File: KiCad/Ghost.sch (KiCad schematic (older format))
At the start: 33 parts, among them P1 MOTOR, P2 SERVO, P3 START, P4 PWM, P5 RGB, Q1 MMBT3904, SW1 BTN1, U1 INA219, U16 Transmissive_Photo_Interrupter, U17 ESP8266_ESP-12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

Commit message: Working on PCB layout for Rev 2
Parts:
- removed P4: PWM, Pin_Headers:Pin_Header_Straight_1x03, symbol CONN_01X03
- removed R27: 3k3, Resistors_SMD:R_0603, symbol R
- added P4: CONN_01X06, Pin_Headers:Pin_Header_Straight_1x06, symbol CONN_01X06
- added R9: 0, Resistors_SMD:R_0603, symbol R
- added SW2: PROG, Buttons_Switches_SMD:SW_SPST_SKQG, symbol SW_PUSH
- D1, D2, D3: footprint LEDs:LED_0805 -> LEDs:LED_0603
- Q1: symbol Q_NPN_BCE -> Q_NPN_BEC
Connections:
- net labels added: FTDI_CTS, FTDI_DTR, FTDI_RX, FTDI_TX, ~WIFI_RESET
- net labels removed: PWM
- wire segments 130 -> 138
- no-connect marks 32 -> 34
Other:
- note added: "Programming header for ESP8266\nUse FTDI Basic.\n0 ohm resistor acts as optional jumper for power."
- note added: "Toggle LEDs with one GPIO\nNPN is a MMBT3904, SOT-23."
- note added: "WiFi. Can be enabled/disabled from Teensy.\nUse pushbutton for firmware programming.\nNB, pull ~Reset~=HIGH and Enable=HIGH using Teensy."
- note removed: "General purpose PWM connector"
- note removed: "Toggle LEDs with one GPIO\nNPN is a MMB3904, SOT-23."
- note removed: "Wireless Network. Can be enabled/disabled."
- moved on the sheet: C2, C3, C9, P3, P5, R25, R26, R28, R29, U16, U3

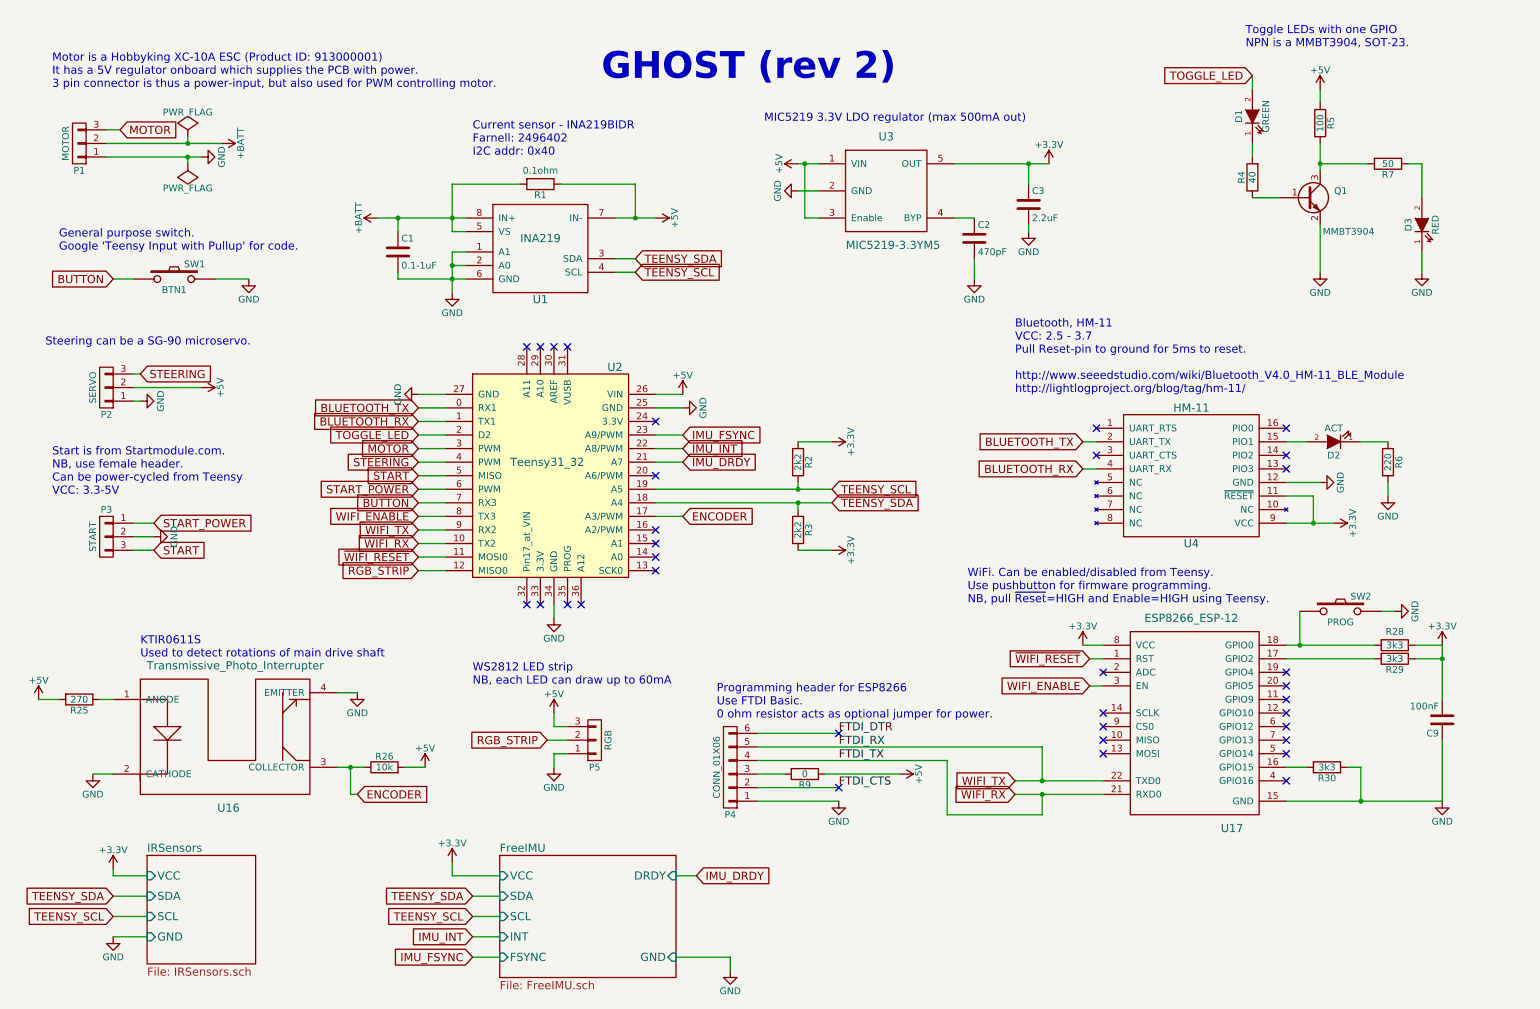
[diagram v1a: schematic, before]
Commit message: Replacing Teensy with ESP8266
Changes made on KiCad on Ubuntu
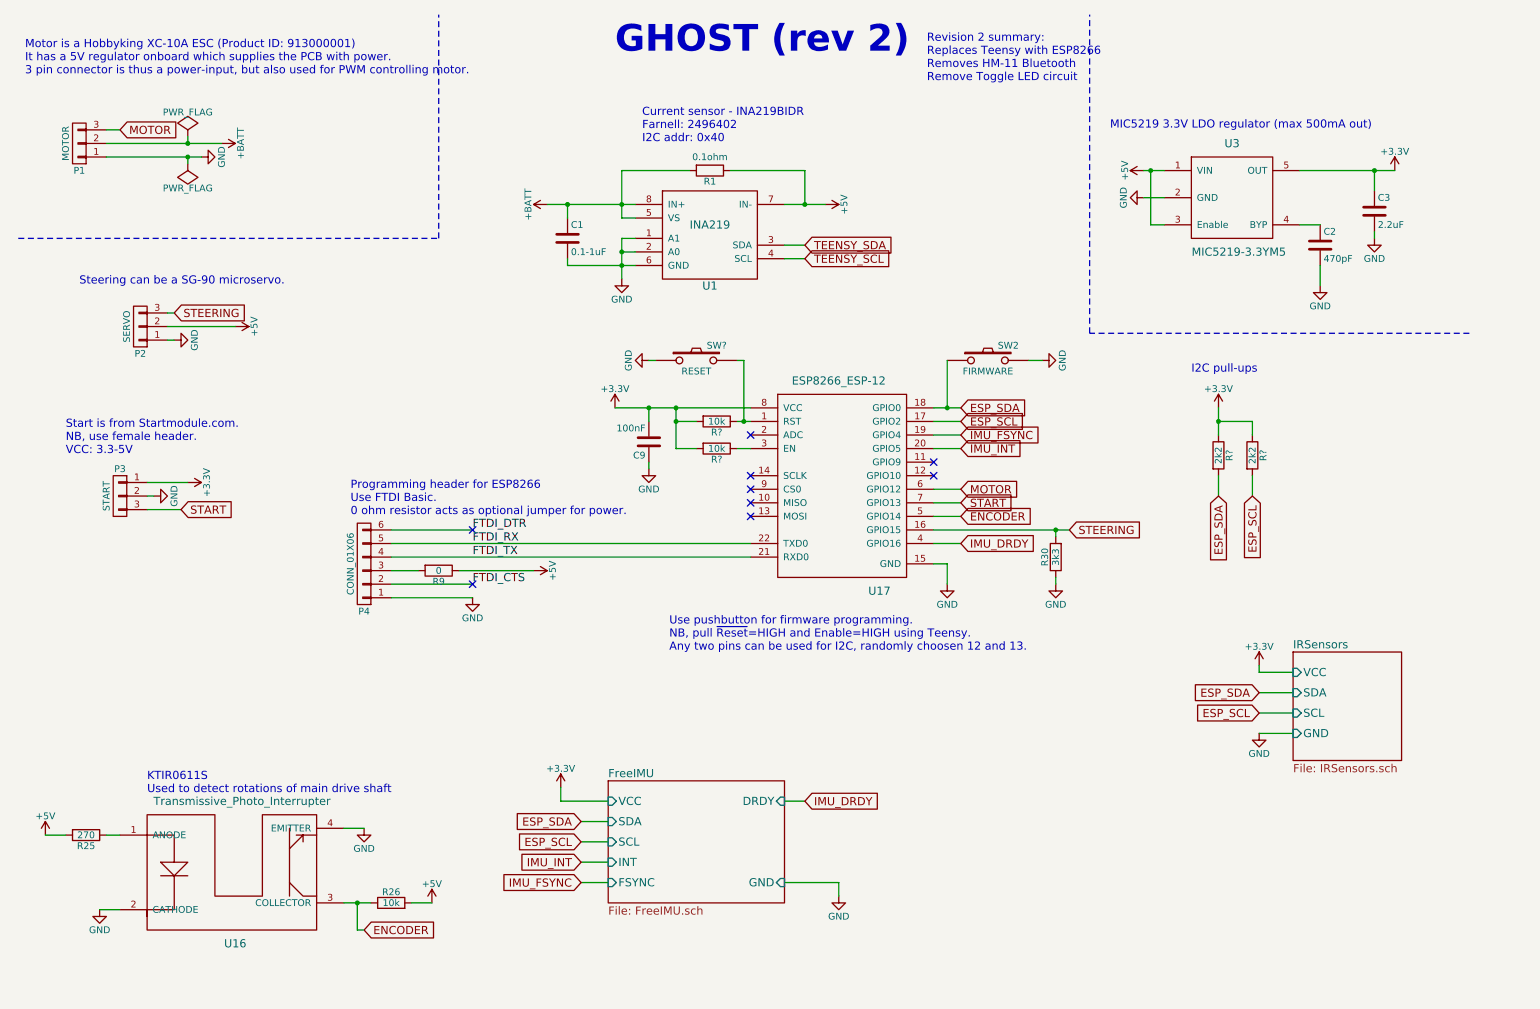
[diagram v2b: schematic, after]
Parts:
- removed D1: GREEN, LEDs:LED_0603, symbol LED
- removed D2: ACT, LEDs:LED_0603, symbol LED
- removed D3: RED, LEDs:LED_0603, symbol LED
- removed P5: RGB, Pin_Headers:Pin_Header_Straight_1x03, symbol CONN_01X03
- removed Q1: MMBT3904, TO_SOT_Packages_SMD:SOT-23, symbol Q_NPN_BEC
- removed R2, R3: 2k2, Resistors_SMD:R_0603, symbol R
- removed R28, R29: 3k3, Resistors_SMD:R_0603, symbol R
- removed R4: 40, Resistors_SMD:R_0603, symbol R
- removed R5: 100, Resistors_SMD:R_0603, symbol R
- removed R6: 220, Resistors_SMD:R_0603, symbol R
- removed R7: 50, Resistors_SMD:R_0603, symbol R
- removed SW1: BTN1, Buttons_Switches_SMD:SW_SPST_SKQG, symbol SW_PUSH
- removed U2: Teensy31_32, NorBotKiCadFootprints:Teensy-3.1_3.2, symbol Teensy31_32
- removed U4: HM-11, NorBotKiCadFootprints:HM-11, symbol HM-11
- added R? (x2): 10k, symbol R
- added R? (x2): 2k2, Resistors_SMD:R_0603, symbol R
- added SW?: RESET, Buttons_Switches_SMD:SW_SPST_SKQG, symbol SW_PUSH
- SW2: value PROG -> FIRMWARE
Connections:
- net START_POWER is gone; now on net +3V3: P3.1 (P1)
- net +3V3: now also R?.1, R?.1, R?.2, R?.2
- net ENCODER: now also U17.5 (GPIO14)
- net GND: now also SW?.1
- net IMU_DRDY: now also U17.4 (GPIO16)
- net IMU_FSYNC: now also U17.19 (GPIO4)
- net IMU_INT: now also U17.20 (GPIO5)
- net MOTOR: now also U17.6 (GPIO12)
- net START: now also U17.7 (GPIO13)
- net STEERING: now also R30.2, U17.16 (GPIO15)
- net ESP_SCL: now reaches U17.17 (GPIO2)
- net ESP_SCL: now also R?.2
- net ESP_SDA: now reaches SW2.1, U17.18 (GPIO0)
- net ESP_SDA: now also R?.2
- net WIFI_ENABLE: no longer names the net of U17.3 (EN)
- net WIFI_ENABLE: now also R?.1
- net WIFI_RX renamed FTDI_TX
- net WIFI_TX renamed FTDI_RX
- net ~WIFI_RESET: no longer names the net of U17.1 (RST)
- net ~WIFI_RESET: now also R?.1, SW?.2
- no-connect marks 34 -> 9
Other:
- note added: "I2C pull-ups"
- note added: "Revision 2 summary: \nReplaces Teensy with ESP8266\nRemoves HM-11 Bluetooth\nRemove Toggle LED circuit"
- note added: "Start is from Startmodule.com.\nNB, use female header.\nVCC: 3.3-5V"
- note added: "Use pushbutton for firmware programming.\nNB, pull ~Reset~=HIGH and Enable=HIGH using Teensy.\nAny two pins can be used for I2C, randomly choosen 12 and 13."
- note removed: "Bluetooth, HM-11\nVCC: 2.5 - 3.7\nPull Reset-pin to ground for 5ms to reset.\n\nhttp://www.seeedstudio.com/wiki/Bluetooth_V4.0_HM-11_BLE_Module\nhttp://lightlogproject.org/blog/tag/hm-11/"
- note removed: "General purpose switch.\nGoogle 'Teensy Input with Pullup' for code."
- note removed: "Start is from Startmodule.com.\nNB, use female header.\nCan be power-cycled from Teensy\nVCC: 3.3-5V"
- note removed: "Toggle LEDs with one GPIO\nNPN is a MMBT3904, SOT-23."
- note removed: "WS2812 LED strip\nNB, each LED can draw up to 60mA"
- note removed: "WiFi. Can be enabled/disabled from Teensy.\nUse pushbutton for firmware programming.\nNB, pull ~Reset~=HIGH and Enable=HIGH using Teensy."
- moved on the sheet: C1, C2, C3, C9, P2, P3, P4, R1, R25, R26, R30, R9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

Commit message: Switching to ESP-WROOM-32
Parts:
- removed P4: CONN_01X06, Pin_Headers:Pin_Header_Straight_1x06, symbol CONN_01X06
- removed R30: 3k3, Resistors_SMD:R_0603, symbol R
- removed R? (x2): 10k, symbol R
- removed SW?: RESET, Buttons_Switches_SMD:SW_SPST_SKQG, symbol SW_PUSH
- removed U17: ESP8266_ESP-12, NorBotKiCadFootprints:ESP8266_ESP_12E, symbol ESP8266_ESP-12
- added C10: 1uF, Capacitors_SMD:C_0603, symbol C
- added C11, C12, C13: 1nF, Capacitors_SMD:C_0603, symbol C
- added D?: SSA33L (Schottky), symbol D_Schottky_Small_ALT
- added P?: USB_OTG, symbol USB_OTG
- added R2: 12K, Resistors_SMD:R_0603, symbol R
- added R3, R4: 5K, Resistors_SMD:R_0603, symbol R
- added R7: 470, Resistors_SMD:R_0603, symbol R
- added SW1: BOOT, Buttons_Switches_SMD:SW_SPST_SKQG, symbol SW_PUSH
- added U2: ESP-WROOM-32, symbol ESP-WROOM-32
- C9: value 100nF -> 100uF
- R9: value 0 -> 470
- SW2: value FIRMWARE -> EN
- gave numbers to parts that had none: 2
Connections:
- net +3V3: now also C9.1, C10.1, R2.1, R4.1, U2.2 (3V3); no longer C9.2
- net +5V: now also D?.1 (K); no longer R9.1
- net ENCODER: now also U2.8 (IO32)
- net ESP_SCL: now also U2.36 (IO22)
- net ESP_SDA: now also U2.37 (IO23); no longer SW2.1
- net GND: now also C9.2, SW2.1, C10.2, C11.2, C12.2, C13.2, R3.2, SW1.1, U2.1 (GND), U2.15 (GND), U2.38 (GND), U2.39 (GND-PAD); no longer C9.1, SW2.2
- net IMU_DRDY: now also U2.29 (IO5)
- net IMU_FSYNC: now also U2.31 (IO19)
- net IMU_INT: now also U2.30 (IO18)
- net MOTOR: now also U2.6 (IO34)
- net START: now also U2.7 (IO35)
- net STEERING: now also U2.9 (IO33)
- net at R9.2: now also SW2.2, C13.1
- new net: C12.1, R7.2, SW1.2
- new net: D?.2 (A), P?.1 (VBUS)
- new net ESP_EN: C11.1, R2.2, R9.1, U2.3 (EN)
- new net ESP_IO0: R4.2, R7.1, U2.25 (IO0)
- new net ESP_IO2: R3.1, U2.24 (IO2)
- no-connect marks 9 -> 0
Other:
- note added: "(add USB bridge here)"
- note added: "Micro-USB connector. Can power the board.\n"
- note added: "Switches for ESP-WROOM-32"
- note removed: "Programming header for ESP8266\nUse FTDI Basic.\n0 ohm resistor acts as optional jumper for power."
- note removed: "Use pushbutton for firmware programming.\nNB, pull ~Reset~=HIGH and Enable=HIGH using Teensy.\nAny two pins can be used for I2C, randomly choosen 12 and 13."
- moved on the sheet: P3, R5, R6

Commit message: More related to USB
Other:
- note added: "(add CP2102 USB bridge here)"
- note added: "Current sensor - INA219BIDR\nFarnell: 249-6402\nI2C addr: 0x40"
- note removed: "(add USB bridge here)"
- note removed: "Current sensor - INA219BIDR\nFarnell: 2496402\nI2C addr: 0x40"
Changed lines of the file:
@@
 $Descr A4 11693 8268
 encoding utf-8
-Sheet 1 3
+Sheet 1 4
 Title "Ghost - Folkracer"
 Date "2016-05-27"
@@
 $EndSheet
 Text Notes 5100 1450 0    60   ~ 0
-Current sensor - INA219BIDR\nFarnell: 2496402\nI2C addr: 0x40
+Current sensor - INA219BIDR\nFarnell: 249-6402\nI2C addr: 0x40
 $Comp
 L GND #PWR17
@@
 	8800 1850 8950 1850
 Wire Wire Line
-	8800 1650 8950 1650
+	8800 1650 8850 1650
+Wire Wire Line
+	8850 1650 8950 1650
 Wire Wire Line
 	8950 2050 8850 2050
@@
 	10500 1800 10500 1650
 Wire Wire Line
-	9950 1650 10650 1650
+	9950 1650 10500 1650
+Wire Wire Line
+	10500 1650 10650 1650
 Connection ~ 10500 1650
 $Comp
@@
 	1150 1350 1250 1350
 Wire Wire Line
-	1150 1550 1850 1550
+	1150 1550 1750 1550
+Wire Wire Line
+	1750 1550 1850 1550
 Wire Wire Line
 	1650 2700 1600 2700
@@
 $EndComp
 Wire Wire Line
-	4400 1900 5050 1900
+	4400 1900 4550 1900
+Wire Wire Line
+	4550 1900 4950 1900
+Wire Wire Line
+	4950 1900 5050 1900
 Wire Wire Line
 	4950 1650 5450 1650
@@
 	6300 1650 6300 1900
 Wire Wire Line
-	6150 1900 6450 1900
+	6150 1900 6300 1900
+Wire Wire Line
+	6300 1900 6450 1900
 Connection ~ 6300 1900
 Wire Wire Line
@@
 	4950 2000 5050 2000
 Wire Wire Line
-	4950 1650 4950 2000
-Wire Wire Line
-	4950 2150 4950 2450
-Wire Wire Line
-	4550 2350 5050 2350
+	4950 1650 4950 1900
+Wire Wire Line
+	4950 1900 4950 2000
+Wire Wire Line
+	4950 2150 4950 2250
+Wire Wire Line
+	4950 2250 4950 2350
+Wire Wire Line
+	4950 2350 4950 2450
+Wire Wire Line
+	4550 2350 4950 2350
+Wire Wire Line
+	4950 2350 5050 2350
 Wire Wire Line
 	5050 2250 4950 2250
@@
 	4550 2300 4550 2350
 Wire Wire Line
-	1150 1450 2000 1450
+	1150 1450 1750 1450
+Wire Wire Line
+	1750 1450 2000 1450
 $Comp
 L PWR_FLAG #FLG1
@@
 ENCODER
 Wire Wire Line
-	2900 7050 3100 7050
+	2900 7050 3000 7050
+Wire Wire Line
+	3000 7050 3100 7050
 Wire Wire Line
 	3050 7250 3000 7250
@@
 	7850 5950 7850 5800
 Wire Wire Line
-	7850 5300 7850 5500
+	7850 5300 7850 5400
+Wire Wire Line
+	7850 5400 7850 5500
 Wire Wire Line
 	8100 5500 8100 5400
@@
 $EndComp
 Wire Wire Line
-	3650 3350 4650 3350
+	3650 3350 3950 3350
+Wire Wire Line
+	3950 3350 4650 3350
 Connection ~ 3950 3350
 Wire Wire Line
@@
 $EndComp
 Wire Wire Line
-	4250 3450 4650 3450
-Wire Wire Line
-	4350 3450 4350 3200
+	4250 3450 4350 3450
+Wire Wire Line
+	4350 3450 4650 3450
+Wire Wire Line
+	4350 3450 4350 3250
+Wire Wire Line
+	4350 3250 4350 3200
 Wire Wire Line
 	4350 2900 4350 2850
@@
 $EndComp
 Wire Wire Line
-	6100 5150 6100 5250
+	6100 5150 6100 5200
+Wire Wire Line
+	6100 5200 6100 5250
 Wire Wire Line
 	6100 5550 6100 5600
@@
 $EndComp
 Wire Wire Line
-	6550 4500 6750 4500
+	6550 4500 6700 4500
+Wire Wire Line
+	6700 4500 6750 4500
 $Comp
 L +3.3V #PWR22
@@
 $EndComp
 Wire Wire Line
-	9900 3350 10050 3350
+	9900 3350 9950 3350
+Wire Wire Line
+	9950 3350 10050 3350
 Wire Wire Line
 	9300 3350 9200 3350
 Wire Wire Line
-	9200 3350 9200 3700
+	9200 3350 9200 3600
+Wire Wire Line
+	9200 3600 9200 3700
 $Comp
 L C C12
@@
 $EndComp
 Wire Wire Line
-	9900 4050 10050 4050
+	9900 4050 9950 4050
+Wire Wire Line
+	9950 4050 10050 4050
 Wire Wire Line
 	9300 4050 9200 4050
 Wire Wire Line
-	9200 4050 9200 4400
+	9200 4050 9200 4300
+Wire Wire Line
+	9200 4300 9200 4400
 $Comp
 L C C13
@@
 	1900 5000 2200 5000
 Text Notes 2250 5300 0    60   ~ 0
-(add USB bridge here)
+(add CP2102 USB bridge here)
+$Sheet
+S 2350 5700 500  150
+U 58929DA4
+F0 "USB" 60
+F1 "USB.sch" 60
+$EndSheet
 $EndSCHEMATC
